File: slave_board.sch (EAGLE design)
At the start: 159 parts, among them IC3 ATMEGA2560-16AU, J11 1935161, J17 RJ45, J22 RJ45, J3 1935161, J6 1935161, K1 ORWH-SH-112D1F, Q1 PHB45NQ15T, Q2 PHB45NQ15T, Q3 BSS138L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

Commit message: board progress
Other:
- note added: "Notes: mounting holes need filter on current sense output? elevator extend copper (GND return path is bad)"
- note removed: "Notes: Damping resistors on SPI for ICSP? 10k resistor array? need filter on current sense output?"
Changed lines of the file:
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@@
 <layers>
 <layer number="1" name="Top" color="4" fill="1" visible="no" active="no"/>
-<layer number="2" name="Route2" color="1" fill="3" visible="no" active="no"/>
-<layer number="3" name="Route3" color="4" fill="3" visible="no" active="no"/>
-<layer number="4" name="Route4" color="1" fill="4" visible="no" active="no"/>
-<layer number="5" name="Route5" color="4" fill="4" visible="no" active="no"/>
-<layer number="6" name="Route6" color="1" fill="8" visible="no" active="no"/>
-<layer number="7" name="Route7" color="4" fill="8" visible="no" active="no"/>
-<layer number="8" name="Route8" color="1" fill="2" visible="no" active="no"/>
-<layer number="9" name="Route9" color="4" fill="2" visible="no" active="no"/>
-<layer number="10" name="Route10" color="1" fill="7" visible="no" active="no"/>
-<layer number="11" name="Route11" color="4" fill="7" visible="no" active="no"/>
-<layer number="12" name="Route12" color="1" fill="5" visible="no" active="no"/>
-<layer number="13" name="Route13" color="4" fill="5" visible="no" active="no"/>
-<layer number="14" name="Route14" color="1" fill="6" visible="no" active="no"/>
-<layer number="15" name="Route15" color="4" fill="6" visible="no" active="no"/>
+<layer number="2" name="Route2" color="16" fill="1" visible="no" active="no"/>
+<layer number="3" name="Route3" color="17" fill="1" visible="no" active="no"/>
+<layer number="4" name="Route4" color="18" fill="1" visible="no" active="no"/>
+<layer number="5" name="Route5" color="19" fill="1" visible="no" active="no"/>
+<layer number="6" name="Route6" color="25" fill="1" visible="no" active="no"/>
+<layer number="7" name="Route7" color="26" fill="1" visible="no" active="no"/>
+<layer number="8" name="Route8" color="27" fill="1" visible="no" active="no"/>
+<layer number="9" name="Route9" color="28" fill="1" visible="no" active="no"/>
+<layer number="10" name="Route10" color="29" fill="1" visible="no" active="no"/>
+<layer number="11" name="Route11" color="30" fill="1" visible="no" active="no"/>
+<layer number="12" name="Route12" color="20" fill="1" visible="no" active="no"/>
+<layer number="13" name="Route13" color="21" fill="1" visible="no" active="no"/>
+<layer number="14" name="Route14" color="22" fill="1" visible="no" active="no"/>
+<layer number="15" name="Route15" color="23" fill="1" visible="no" active="no"/>
 <layer number="16" name="Bottom" color="1" fill="1" visible="no" active="no"/>
 <layer number="17" name="Pads" color="2" fill="1" visible="no" active="no"/>
-<layer number="18" name="Vias" color="14" fill="1" visible="no" active="no"/>
+<layer number="18" name="Vias" color="2" fill="1" visible="no" active="no"/>
 <layer number="19" name="Unrouted" color="6" fill="1" visible="no" active="no"/>
-<layer number="20" name="Dimension" color="15" fill="1" visible="no" active="no"/>
+<layer number="20" name="Dimension" color="24" fill="1" visible="no" active="no"/>
 <layer number="21" name="tPlace" color="7" fill="1" visible="no" active="no"/>
 <layer number="22" name="bPlace" color="7" fill="1" visible="no" active="no"/>
@@
 <layer number="27" name="tValues" color="7" fill="1" visible="no" active="no"/>
 <layer number="28" name="bValues" color="7" fill="1" visible="no" active="no"/>
-<layer number="29" name="tStop" color="2" fill="3" visible="no" active="no"/>
-<layer number="30" name="bStop" color="5" fill="6" visible="no" active="no"/>
+<layer number="29" name="tStop" color="7" fill="3" visible="no" active="no"/>
+<layer number="30" name="bStop" color="7" fill="6" visible="no" active="no"/>
 <layer number="31" name="tCream" color="7" fill="4" visible="no" active="no"/>
 <layer number="32" name="bCream" color="7" fill="5" visible="no" active="no"/>
@@
 <layer number="47" name="Measures" color="7" fill="1" visible="no" active="no"/>
 <layer number="48" name="Document" color="7" fill="1" visible="no" active="no"/>
-<layer number="49" name="Reference" color="13" fill="1" visible="no" active="no"/>
+<layer number="49" name="Reference" color="7" fill="1" visible="no" active="no"/>
 <layer number="50" name="dxf" color="12" fill="1" visible="no" active="no"/>
 <layer number="51" name="tDocu" color="7" fill="1" visible="no" active="no"/>
@@
 <text x="-147.32" y="160.02" size="1.778" layer="91"></text>
 <text x="327.66" y="236.22" size="1.778" layer="91">Notes:
-Damping resistors on SPI for ICSP?
-10k resistor array?
+mounting holes
 need filter on current sense output?
-</text>
+elevator extend copper (GND return path is bad)</text>
 <text x="342.9" y="162.56" size="1.778" layer="97">JP1 = VDDA-to-VDDB connection
 Closed by Default

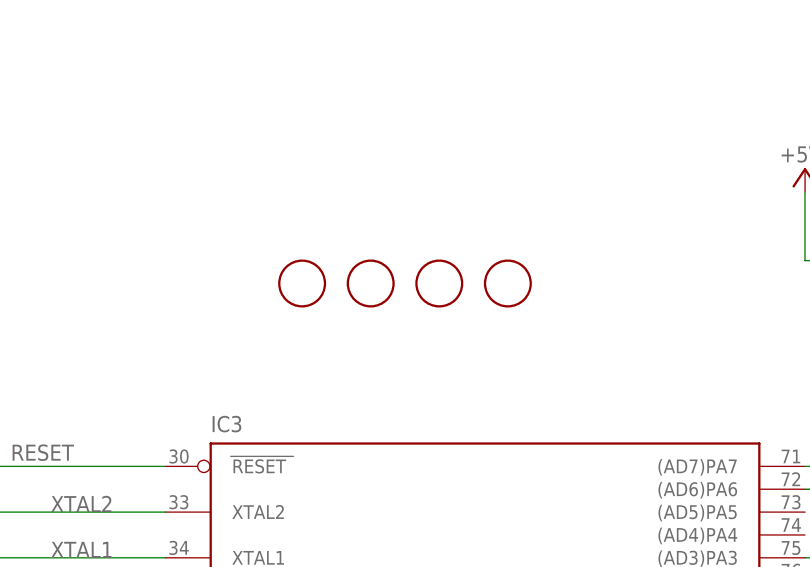
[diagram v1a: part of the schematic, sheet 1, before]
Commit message: Resize board, add mounting holes
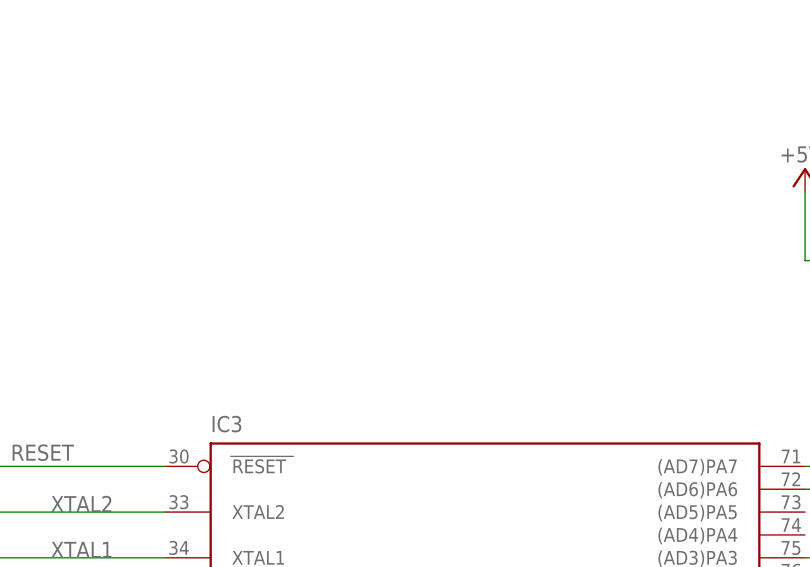
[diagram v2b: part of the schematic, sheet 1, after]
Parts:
- removed FD1, FD2, FD3, FD4: FIDUCIALMOUNT, SmartPrj:FIDUCIALMOUNT
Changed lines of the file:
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@@
 <part name="GND14" library="supply1" library_urn="urn:adsk.eagle:library:371" deviceset="GND" device=""/>
 <part name="P+5" library="supply1" library_urn="urn:adsk.eagle:library:371" deviceset="+5V" device=""/>
-<part name="FD1" library="SmartPrj" deviceset="FIDUCIALMOUNT" device=""/>
-<part name="FD2" library="SmartPrj" deviceset="FIDUCIALMOUNT" device=""/>
-<part name="FD3" library="SmartPrj" deviceset="FIDUCIALMOUNT" device=""/>
 <part name="C3" library="rcl" library_urn="urn:adsk.eagle:library:334" deviceset="C-US" device="C0603" package3d_urn="urn:adsk.eagle:package:23616/2" value="100n"/>
 <part name="GND8" library="supply1" library_urn="urn:adsk.eagle:library:371" deviceset="GND" device=""/>
@@
 <part name="GND23" library="supply1" library_urn="urn:adsk.eagle:library:371" deviceset="GND" device=""/>
 <part name="GND20" library="supply1" library_urn="urn:adsk.eagle:library:371" deviceset="GND" device=""/>
-<part name="FD4" library="SmartPrj" deviceset="FIDUCIALMOUNT" device=""/>
 <part name="Y1" library="ABLS-16.000MHZ-B4-T" deviceset="ABLS-16.000MHZ-B4-T" device=""/>
 <part name="S1" library="FSM2JSMA" deviceset="FSM2JSMA" device=""/>
@@
 <attribute name="VALUE" x="207.645" y="223.52" size="1.778" layer="96" rot="R180"/>
 </instance>
-<instance part="FD1" gate="G$1" x="149.86" y="208.28" smashed="yes"/>
-<instance part="FD2" gate="G$1" x="157.48" y="208.28" smashed="yes"/>
-<instance part="FD3" gate="G$1" x="165.1" y="208.28" smashed="yes"/>
 <instance part="C3" gate="G$1" x="106.68" y="144.78" smashed="yes" rot="MR0">
 <attribute name="NAME" x="105.156" y="145.161" size="1.778" layer="95" rot="MR0"/>
@@
 <attribute name="VALUE" x="68.58" y="182.88" size="1.778" layer="96" rot="R270"/>
 </instance>
-<instance part="FD4" gate="G$1" x="172.72" y="208.28" smashed="yes"/>
 <instance part="Y1" gate="G$1" x="91.44" y="182.88" smashed="yes">
 <attribute name="NAME" x="86.35886875" y="185.166509375" size="1.7784" layer="95"/>

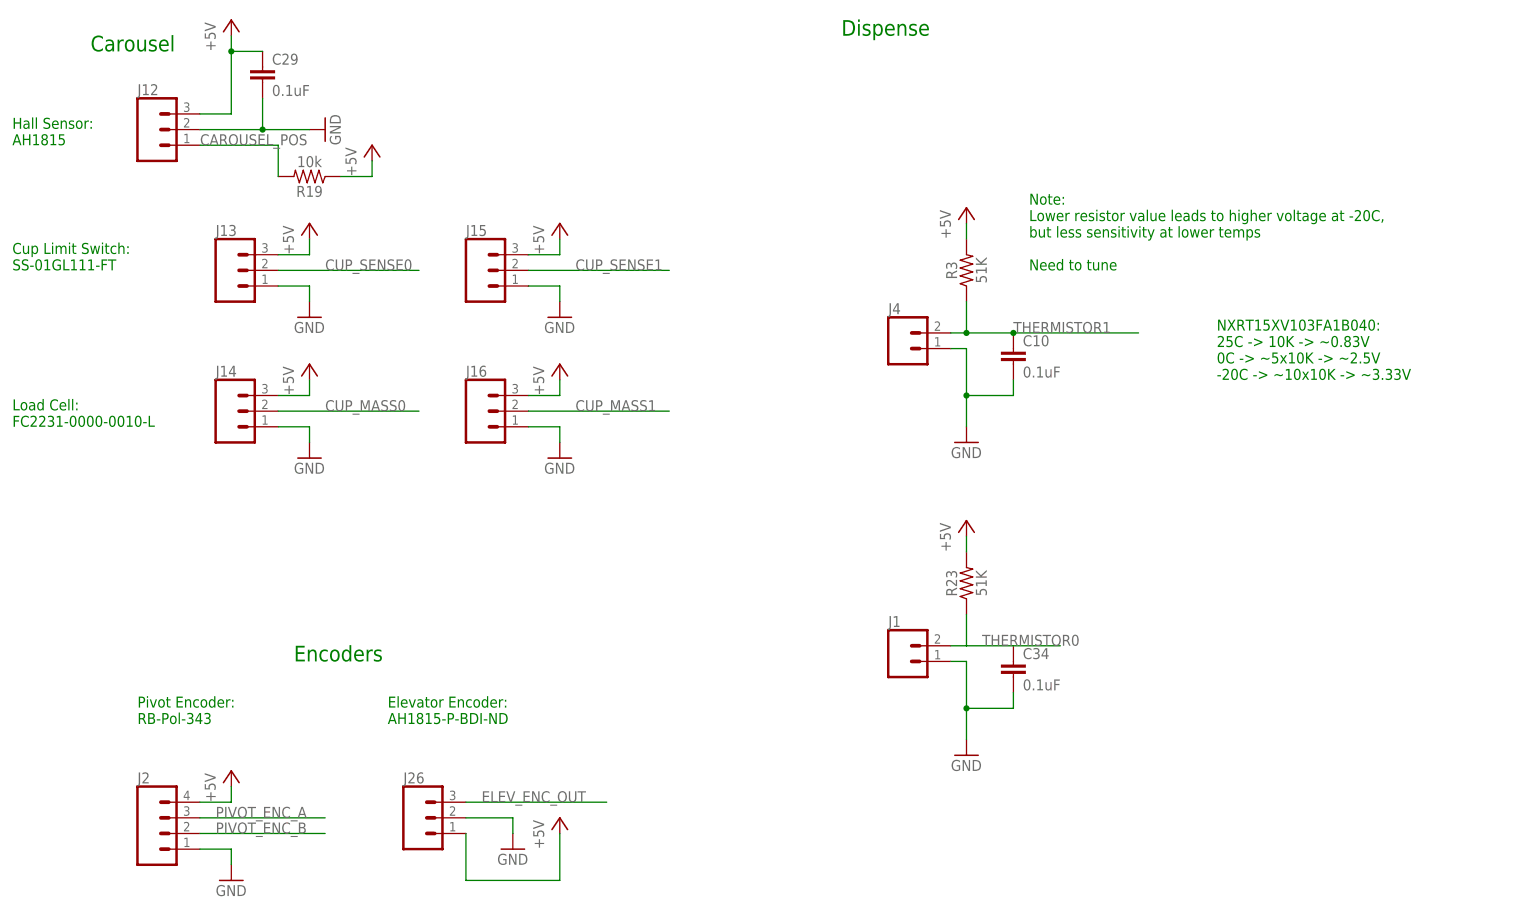
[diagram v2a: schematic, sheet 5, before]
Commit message: Added screw terminal headers
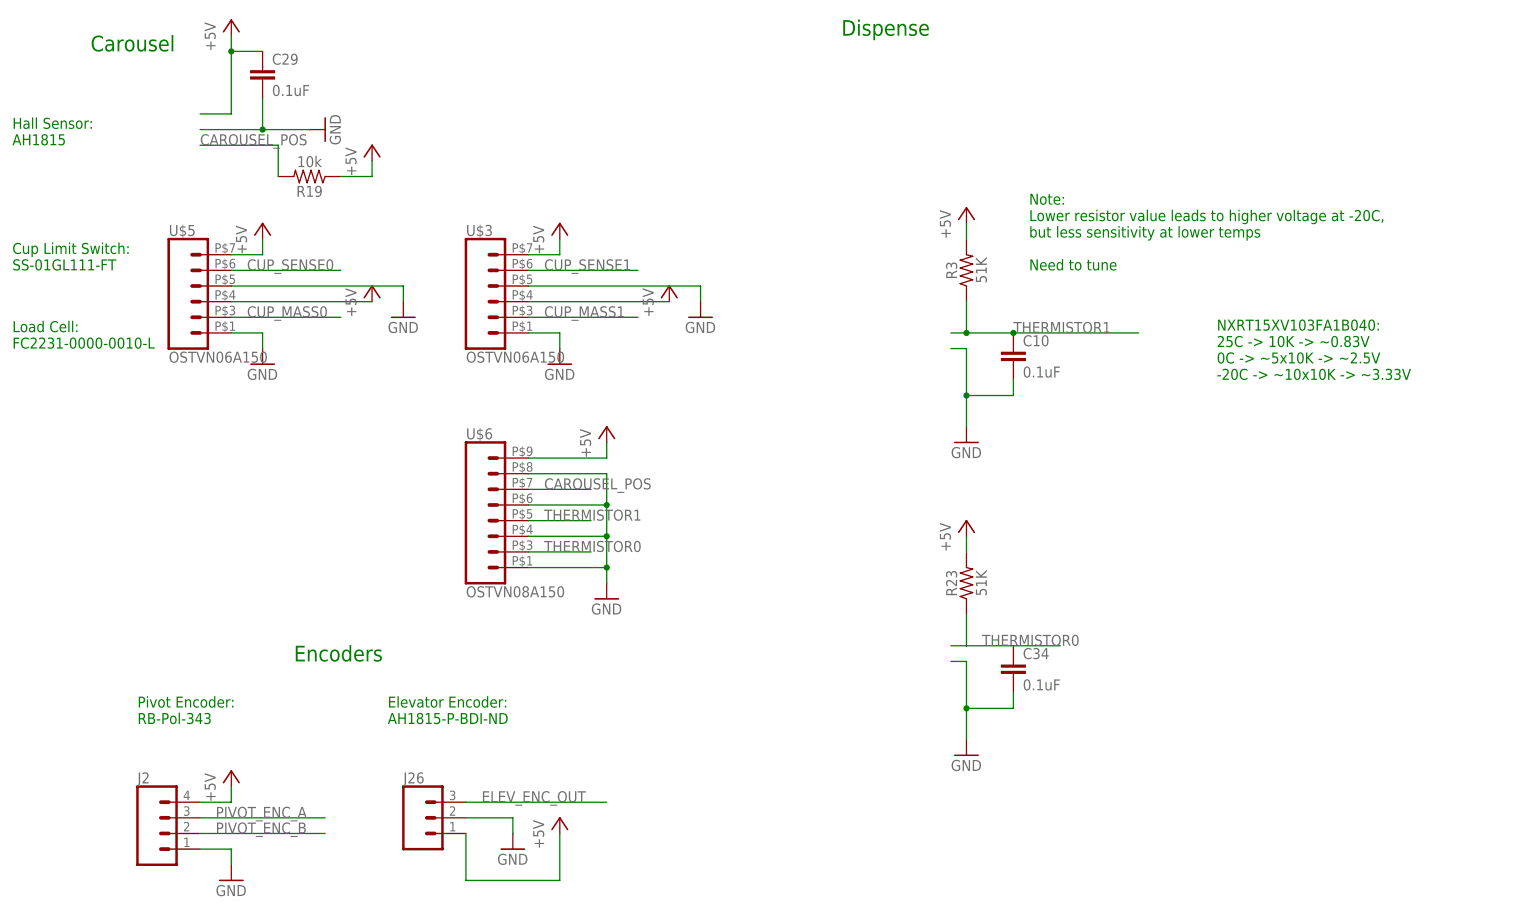
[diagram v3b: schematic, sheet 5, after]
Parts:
- removed J1, J4: (no value), SparkFun-Connectors:CONN_02
- removed J12, J13, J14, J15, J16: (no value), SparkFun-Connectors:CONN_03
- added U$3, U$5: OSTVN06A150, smoothio:OSTVN06A150
- added U$6: OSTVN08A150, smoothio:OSTVN08A150
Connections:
- net +5V: now also U$3.3, U$3.6, U$5.3, U$5.6, U$6.8; no longer J12.3, J13.3, J14.3, J15.3, J16.3
- net CAROUSEL_POS: now also U$6.6; no longer J12.1
- net CUP_MASS0: now also U$5.2; no longer J14.2
- net CUP_MASS1: now also U$3.2; no longer J16.2
- net CUP_SENSE0: now also U$5.5; no longer J13.2
- net CUP_SENSE1: now also U$3.5; no longer J15.2
- net GND: now also U$3.1, U$3.4, U$5.1, U$5.4, U$6.1, U$6.3, U$6.5, U$6.7; no longer J1.1, J12.2, J13.1, J14.1, J15.1, J16.1, J4.1
- net THERMISTOR0: now also U$6.2; no longer J1.2
- net THERMISTOR1: now also U$6.4; no longer J4.2

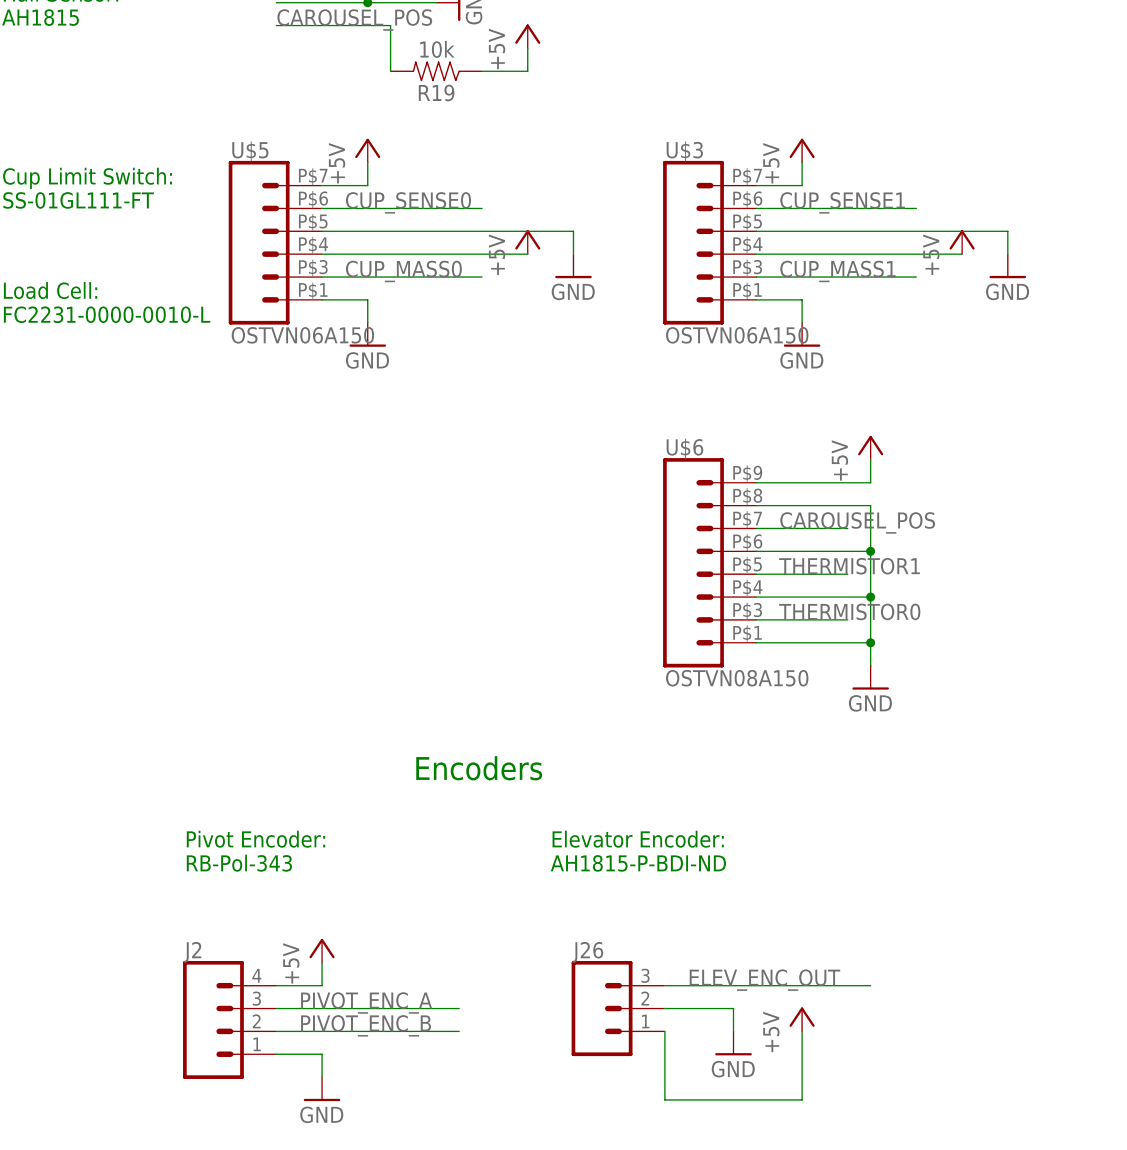
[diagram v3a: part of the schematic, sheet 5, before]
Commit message: Placed another screw terminal
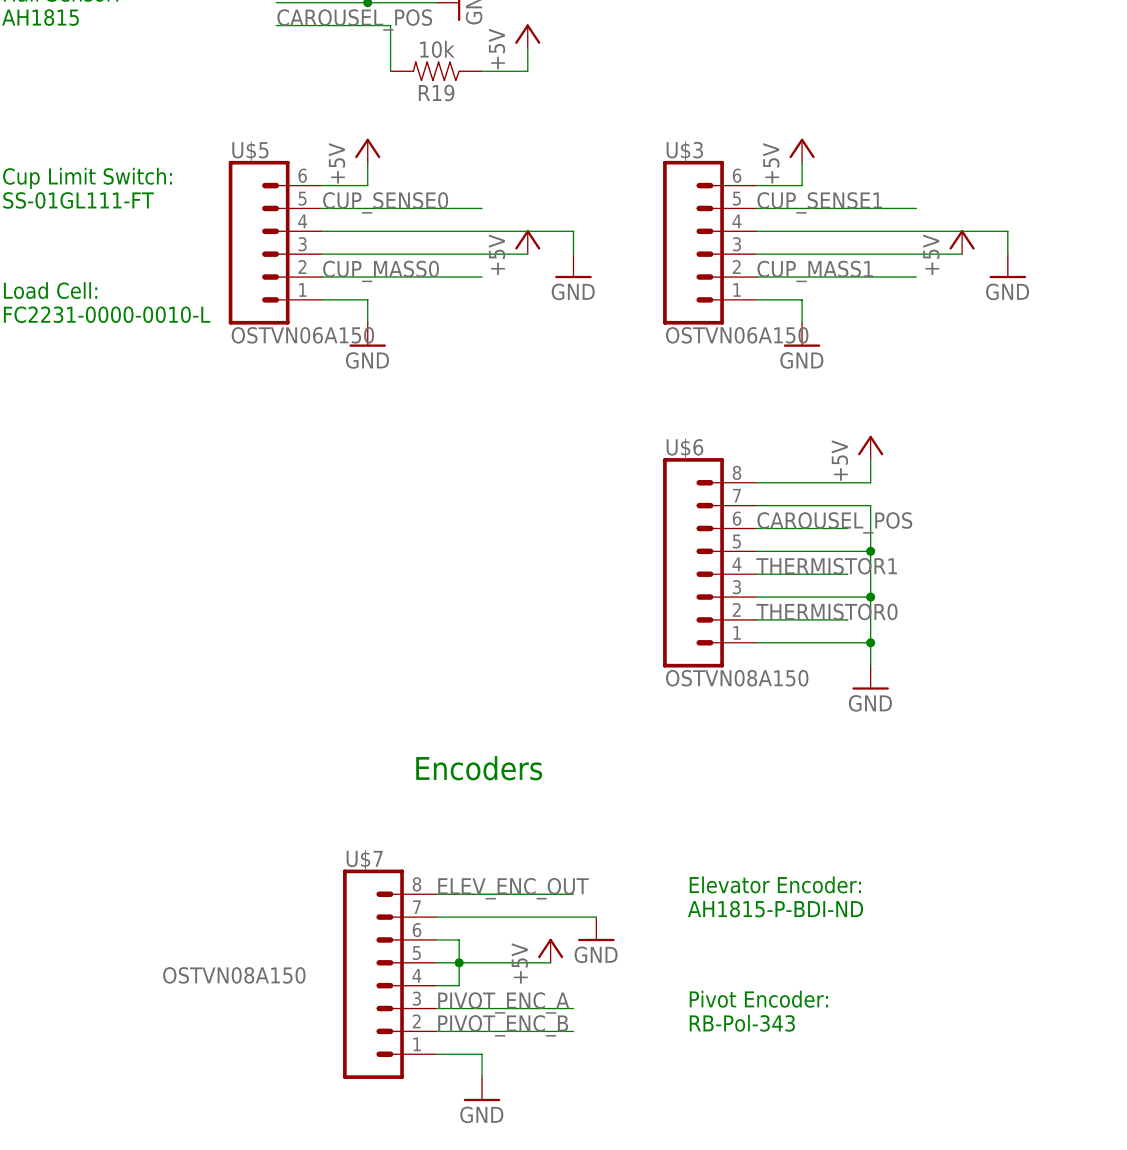
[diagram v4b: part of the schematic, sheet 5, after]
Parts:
- removed J2: (no value), SparkFun-Connectors:CONN_04
- removed J26: (no value), SparkFun-Connectors:CONN_03
- added U$7: OSTVN08A150, smoothio:OSTVN08A150
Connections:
- net +5V: now also U$7.4, U$7.5, U$7.6; no longer J2.4, J26.1
- net ELEV_ENC_OUT: now also U$7.8; no longer J26.3
- net GND: now also U$7.1, U$7.7; no longer J2.1, J26.2
- net PIVOT_ENC_A: now also U$7.3; no longer J2.3
- net PIVOT_ENC_B: now also U$7.2; no longer J2.2
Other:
- moved on the sheet: U$3, U$5, U$6
